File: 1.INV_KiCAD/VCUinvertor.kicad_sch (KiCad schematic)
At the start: 156 parts, among them J10 FAN2, J11 PUMP1, J12 PUMP2, J7 PowerSupply, J8 FAN1, J9 BRAKE LIGHT, K1 IM06DGR, Q1 2N7002, Q10 2N7002, Q11 2N7002, Q12 2N7002, Q13 BC848C, Q14 2N7002, Q15 IRLZ44N, Q16 IRLZ44N, Q17 IRLZ44N, Q18 2N7002, Q19 IRLZ44N, Q2 2N7002, Q3 2N7002, Q4 2N7002, Q5 2N7002, Q6 2N7002, Q7 2N7002, Q8 2N7002, Q9 2N7002, U1 TJA1448ATK, U2 REF3433T, U3 TLV76150DCY

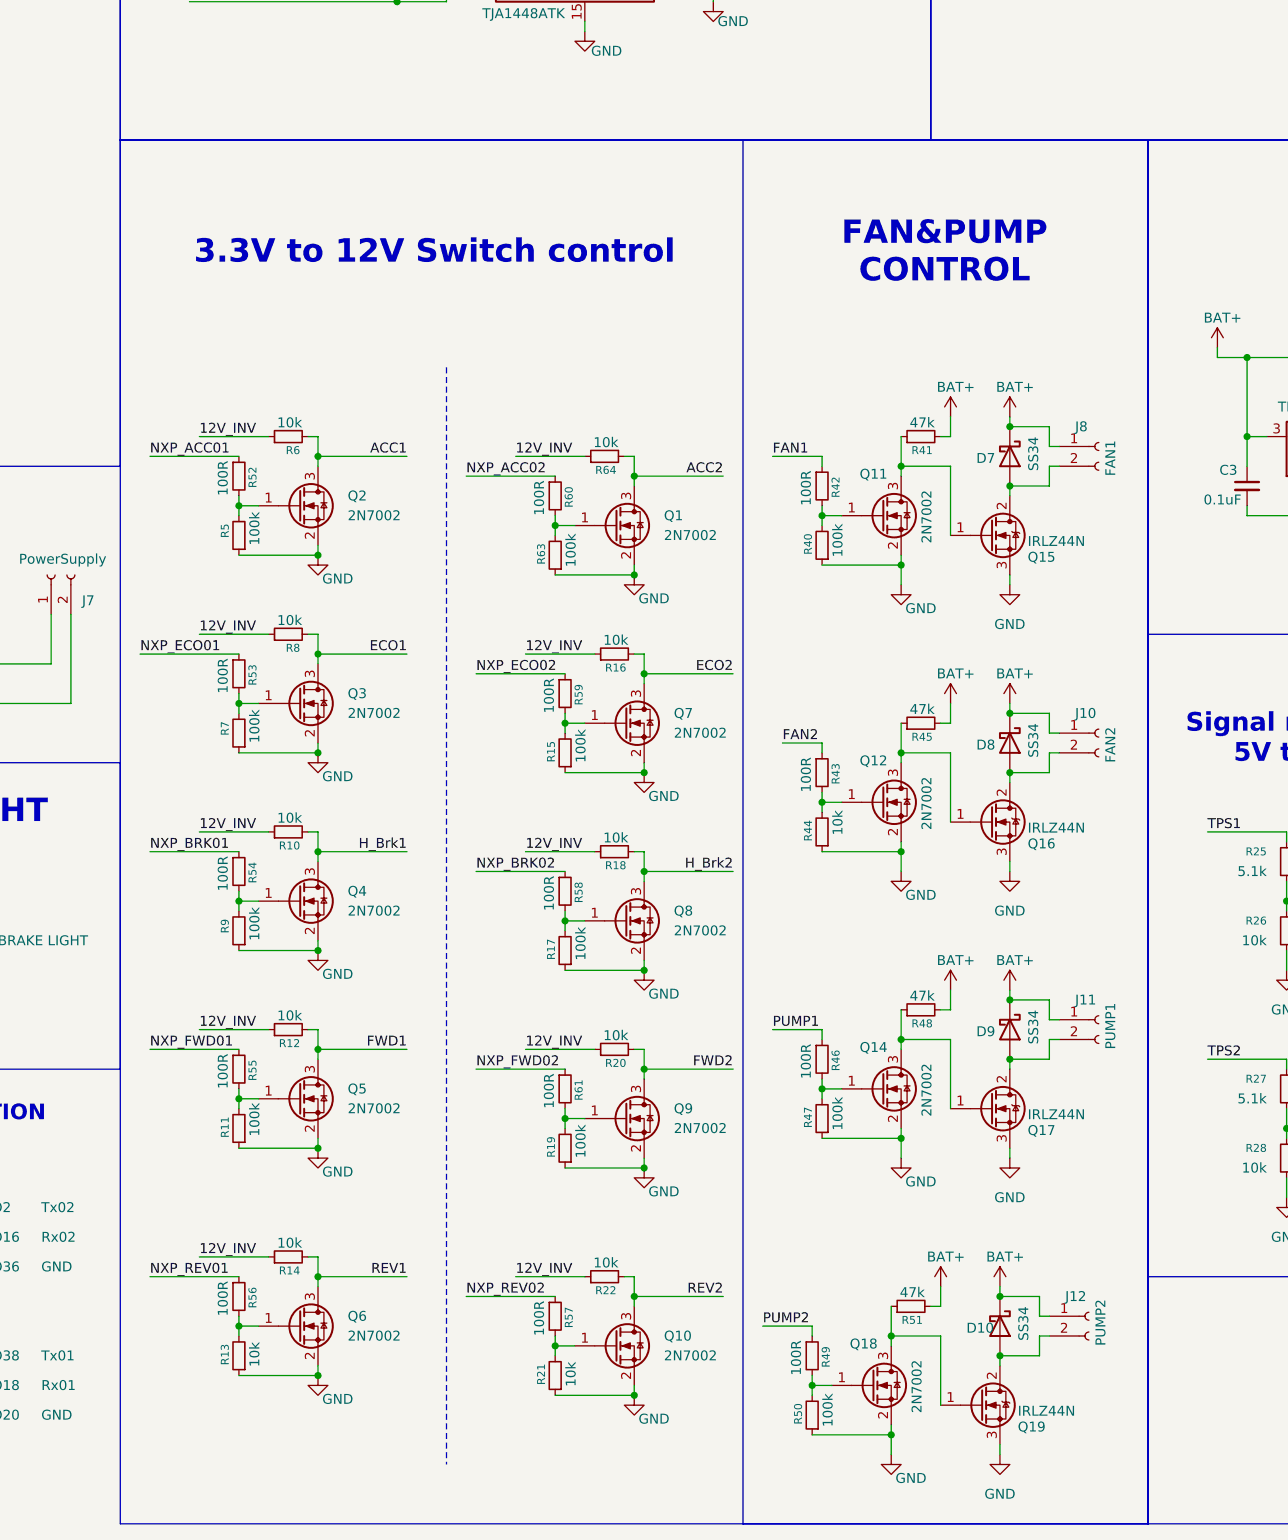
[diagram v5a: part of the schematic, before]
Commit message: Gate Driver MOS added + layout done
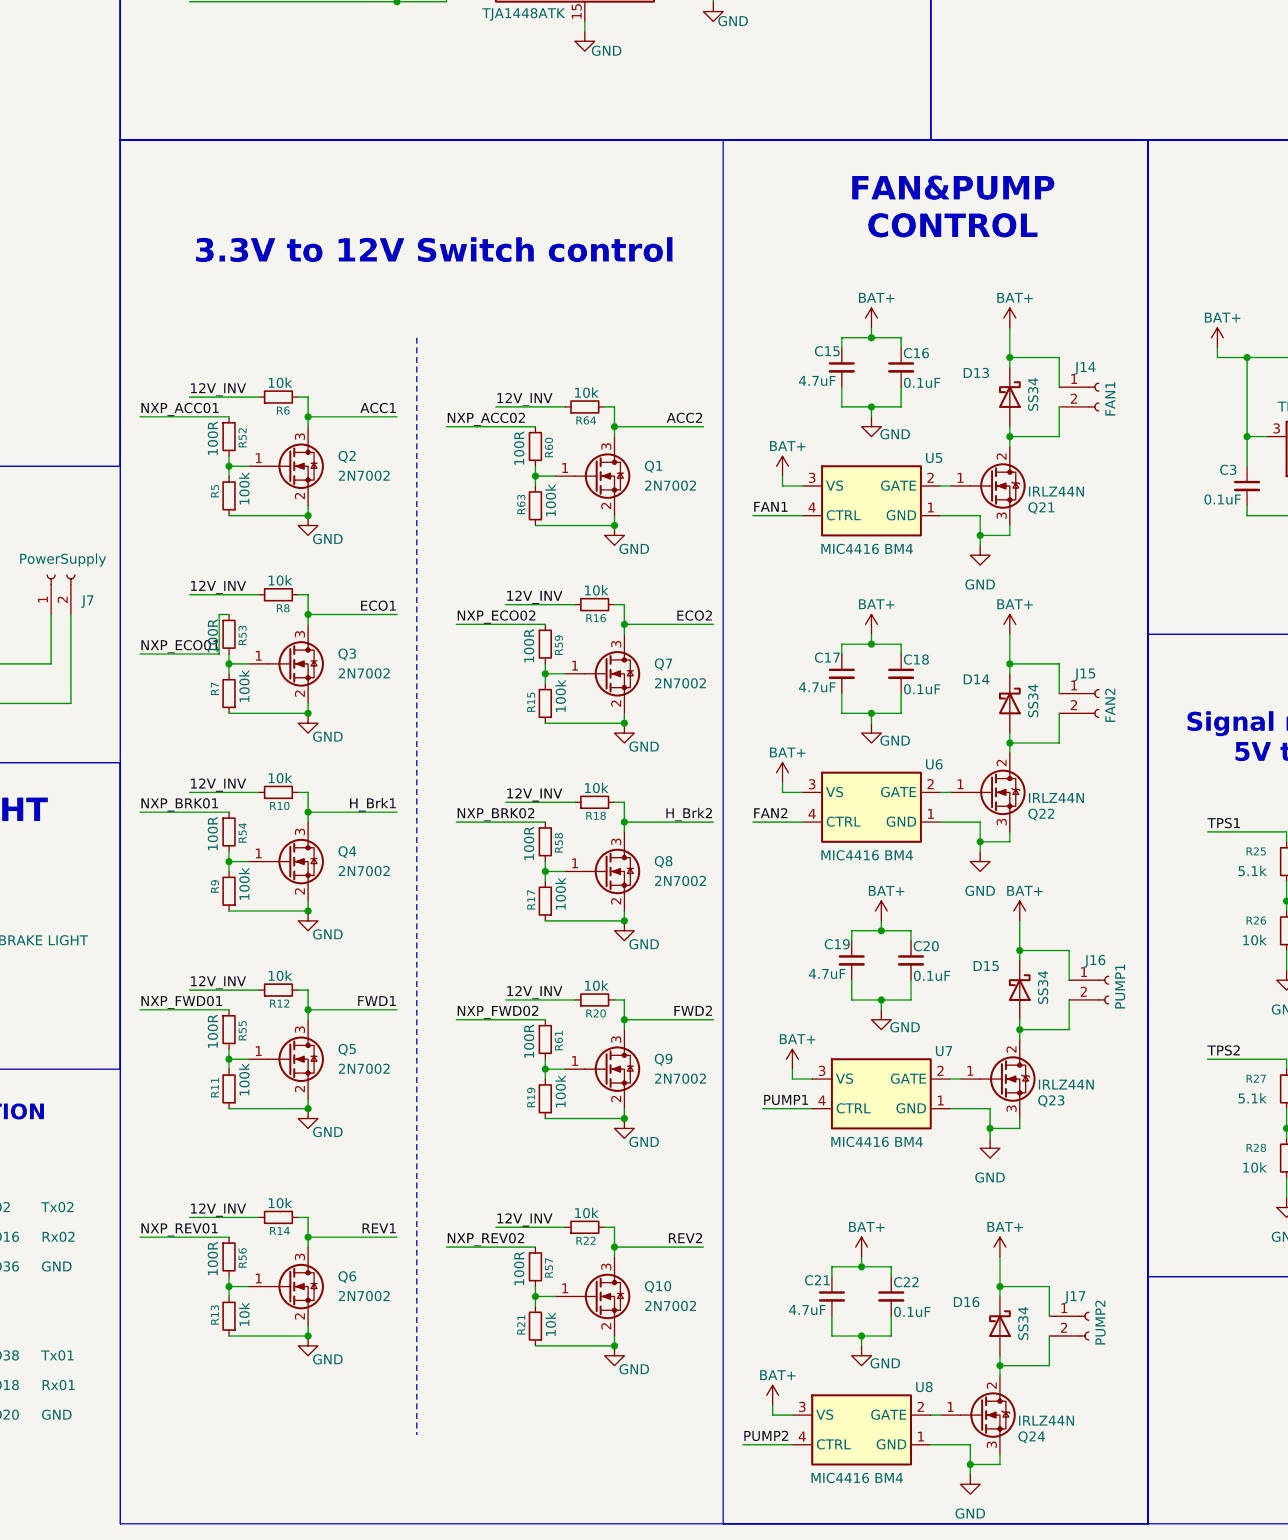
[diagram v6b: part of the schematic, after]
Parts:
- removed D10, D7, D8, D9: SS34, Diode_SMD:D_SMA, symbol Diode:SS34
- removed J10: FAN2, Connector_JST:JST_XH_B2B-XH-A_1x02_P2.50mm_Vertical, symbol Connector:Conn_01x02_Socket
- removed J11: PUMP1, Connector_JST:JST_XH_B2B-XH-A_1x02_P2.50mm_Vertical, symbol Connector:Conn_01x02_Socket
- removed J12: PUMP2, Connector_JST:JST_XH_B2B-XH-A_1x02_P2.50mm_Vertical, symbol Connector:Conn_01x02_Socket
- removed J8: FAN1, Connector_JST:JST_XH_B2B-XH-A_1x02_P2.50mm_Vertical, symbol Connector:Conn_01x02_Socket
- removed Q11, Q12, Q14, Q18: 2N7002, Package_TO_SOT_SMD:SOT-23, symbol Transistor_FET:2N7002
- removed Q15, Q16, Q17, Q19: IRLZ44N, Package_TO_SOT_THT:TO-220-3_Vertical, symbol Transistor_FET:IRLZ44N
- removed R40, R47, R50: 100k, Resistor_SMD:R_1206_3216Metric_Pad1.30x1.75mm_HandSolder, symbol Device:R_Small
- removed R41, R45, R48, R51: 47k, Resistor_SMD:R_1206_3216Metric_Pad1.30x1.75mm_HandSolder, symbol Device:R_Small
- removed R42, R43, R46, R49: 100R, Resistor_SMD:R_1206_3216Metric_Pad1.30x1.75mm_HandSolder, symbol Device:R_Small
- removed R44: 10k, Resistor_SMD:R_1206_3216Metric_Pad1.30x1.75mm_HandSolder, symbol Device:R_Small
- added C15, C17, C19, C21: 4.7uF, Capacitor_SMD:C_1206_3216Metric_Pad1.33x1.80mm_HandSolder, symbol Device:C_Small
- added C16, C18, C20, C22: 0.1uF, Capacitor_SMD:C_1206_3216Metric_Pad1.33x1.80mm_HandSolder, symbol Device:C_Small
- added D13, D14, D15, D16: SS34, Diode_SMD:D_SMA, symbol Diode:SS34
- added J14: FAN1, Connector_JST:JST_XH_B2B-XH-A_1x02_P2.50mm_Vertical, symbol Connector:Conn_01x02_Socket
- added J15: FAN2, Connector_JST:JST_XH_B2B-XH-A_1x02_P2.50mm_Vertical, symbol Connector:Conn_01x02_Socket
- added J16: PUMP1, Connector_JST:JST_XH_B2B-XH-A_1x02_P2.50mm_Vertical, symbol Connector:Conn_01x02_Socket
- added J17: PUMP2, Connector_JST:JST_XH_B2B-XH-A_1x02_P2.50mm_Vertical, symbol Connector:Conn_01x02_Socket
- added Q21, Q22, Q23, Q24: IRLZ44N, Package_TO_SOT_THT:TO-220-3_Vertical, symbol Transistor_FET:IRLZ44N
- added U5, U6, U7, U8: MIC4416 BM4, Package_TO_SOT_SMD:SOT-143_Handsoldering, symbol Driver_FET:MIC4426
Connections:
- net BAT+: now also C15.1, C16.1, C17.1, C18.1, C19.1, C20.1, C21.1, C22.1, D13.1 (K), D14.1 (K), D15.1 (K), D16.1 (K), J14.1 (Pin_1), J15.1 (Pin_1), J16.1 (Pin_1), J17.1 (Pin_1), U5.3 (VS), U6.3 (VS), U7.3 (VS), U8.3 (VS)
- net FAN1: now also U5.4 (CTRL)
- net FAN2: now also U6.4 (CTRL)
- net GND: now also C15.2, C16.2, C17.2, C18.2, C19.2, C20.2, C21.2, C22.2, Q21.3 (S), Q22.3 (S), Q23.3 (S), Q24.3 (S), U5.1 (GND), U6.1 (GND), U7.1 (GND), U8.1 (GND)
- net PUMP1: now also U7.4 (CTRL)
- net PUMP2: now also U8.4 (CTRL)
- new net: Q24.1 (G), U8.2 (GATE)
- new net: D16.2 (A), J17.2 (Pin_2), Q24.2 (D)
- new net: Q23.1 (G), U7.2 (GATE)
- new net: D15.2 (A), J16.2 (Pin_2), Q23.2 (D)
- new net: Q21.1 (G), U5.2 (GATE)
- new net: D14.2 (A), J15.2 (Pin_2), Q22.2 (D)
- new net: Q22.1 (G), U6.2 (GATE)
- new net: D13.2 (A), J14.2 (Pin_2), Q21.2 (D)
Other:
- moved on the sheet: Q1, Q10, Q2, Q3, Q4, Q5, Q6, Q7, Q8, Q9, R10, R11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

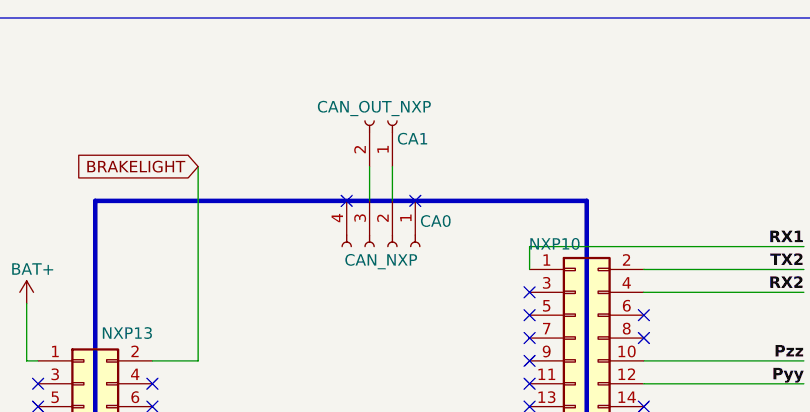
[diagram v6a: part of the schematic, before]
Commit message: CAN_IN + CAN_OUT added
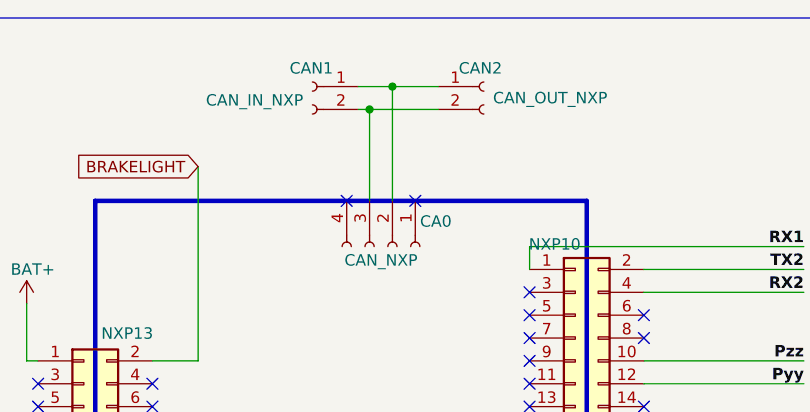
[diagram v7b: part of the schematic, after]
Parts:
- added CAN2: CAN_OUT_NXP, Connector_JST:JST_PH_B2B-PH-K_1x02_P2.00mm_Vertical, symbol Connector:Conn_01x02_Socket
- CAN1: renamed from CA1; value CAN_OUT_NXP -> CAN_IN_NXP; footprint Connector_JST:JST_XH_B2B-XH-A_1x02_P2.50mm_Vertical -> Connector_JST:JST_PH_B2B-PH-K_1x02_P2.00mm_Vertical
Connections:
- net at CA0.2 (Pin_2), CAN1.1 (Pin_1): now also CAN2.1 (Pin_1)
- net at CA0.3 (Pin_3), CAN1.2 (Pin_2): now also CAN2.2 (Pin_2)
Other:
- moved on the sheet: CAN1
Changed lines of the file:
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@@
 	)
 	(junction
+		(at 93.98 20.32)
+		(diameter 0)
+		(color 0 0 0 0)
+	)
+	(junction
 		(at 201.93 64.77)
 		(diameter 0)
@@
 	)
 	(junction
+		(at 91.44 22.86)
+		(diameter 0)
+		(color 0 0 0 0)
+	)
+	(junction
 		(at 191.77 167.64)
 		(diameter 0)
@@
 	(wire
 		(pts
+			(xy 90.17 20.32) (xy 93.98 20.32)
+		)
+		(stroke
+			(width 0)
+			(type default)
+		)
+	)
+	(wire
+		(pts
 			(xy 109.22 38.1) (xy 139.7 38.1)
 		)
@@
 	(wire
 		(pts
-			(xy 91.44 29.21) (xy 91.44 33.02)
-		)
-		(stroke
-			(width 0)
-			(type default)
-		)
-	)
-	(wire
-		(pts
 			(xy 232.41 219.71) (xy 232.41 220.98)
 		)
@@
 	(wire
 		(pts
+			(xy 91.44 22.86) (xy 91.44 33.02)
+		)
+		(stroke
+			(width 0)
+			(type default)
+		)
+	)
+	(wire
+		(pts
 			(xy 353.06 73.66) (xy 358.14 73.66)
 		)
@@
 	(wire
 		(pts
+			(xy 90.17 22.86) (xy 91.44 22.86)
+		)
+		(stroke
+			(width 0)
+			(type default)
+		)
+	)
+	(wire
+		(pts
 			(xy 181.61 154.94) (xy 191.77 154.94)
 		)
@@
 	(wire
 		(pts
+			(xy 91.44 22.86) (xy 99.06 22.86)
+		)
+		(stroke
+			(width 0)
+			(type default)
+		)
+	)
+	(wire
+		(pts
 			(xy 355.6 224.79) (xy 355.6 227.33)
 		)
@@
 	(wire
 		(pts
+			(xy 93.98 20.32) (xy 93.98 33.02)
+		)
+		(stroke
+			(width 0)
+			(type default)
+		)
+	)
+	(wire
+		(pts
 			(xy 127 167.64) (xy 140.97 167.64)
 		)
@@
 	(wire
 		(pts
+			(xy 93.98 20.32) (xy 99.06 20.32)
+		)
+		(stroke
+			(width 0)
+			(type default)
+		)
+	)
+	(wire
+		(pts
 			(xy 25.4 215.9) (xy 25.4 219.71)
 		)
@@
 	(wire
 		(pts
-			(xy 93.98 29.21) (xy 93.98 33.02)
-		)
-		(stroke
-			(width 0)
-			(type default)
-		)
-	)
-	(wire
-		(pts
 			(xy 210.82 168.91) (xy 222.25 168.91)
 		)
@@
 	(symbol
 		(lib_id "Connector:Conn_01x02_Socket")
-		(at 93.98 24.13 270)
-		(mirror x)
+		(at 85.09 20.32 0)
+		(mirror y)
 		(unit 1)
 		(body_style 1)
@@
 		(in_pos_files yes)
 		(dnp no)
-		(property "Reference" "CA1"
-			(at 94.488 26.162 90)
+		(property "Reference" "CAN1"
+			(at 87.376 18.288 0)
 			(show_name no)
 			(do_not_autoplace no)
@@
 			)
 		)
-		(property "Value" "CAN_OUT_NXP"
-			(at 85.598 22.606 90)
+		(property "Value" "CAN_IN_NXP"
+			(at 84.074 21.844 0)
 			(show_name no)
 			(do_not_autoplace no)
@@
 			)
 		)
-		(property "Footprint" "Connector_JST:JST_XH_B2B-XH-A_1x02_P2.50mm_Vertical"
-			(at 93.98 24.13 0)
+		(property "Footprint" "Connector_JST:JST_PH_B2B-PH-K_1x02_P2.00mm_Vertical"
+			(at 85.09 20.32 0)
 			(hide yes)
 			(show_name no)
@@
 		)
 		(property "Datasheet" ""
-			(at 93.98 24.13 0)
+			(at 85.09 20.32 0)
 			(hide yes)
 			(show_name no)
@@
 		)
 		(property "Description" "Generic connector, single row, 01x02, script generated"
-			(at 93.98 24.13 0)
+			(at 85.09 20.32 0)
 			(hide yes)
 			(show_name no)
@@
 			(project "VCUinvertor"
 				(path "/2b4b6758-f217-4dbc-8f9c-9ada5d4e488c"
-					(reference "CA1")
+					(reference "CAN1")
 					(unit 1)
 				)
@@
 					(unit 1)
 				)
+			)
+		)
+	)
+	(symbol
+		(lib_id "Connector:Conn_01x02_Socket")
+		(at 104.14 20.32 0)
+		(unit 1)
+		(body_style 1)
+		(exclude_from_sim no)
+		(in_bom yes)
+		(on_board yes)
+		(in_pos_files yes)
+		(dnp no)
+		(property "Reference" "CAN2"
+			(at 101.346 18.288 0)
+			(show_name no)
+			(do_not_autoplace no)
+			(effects
+				(font
+					(size 1.27 1.27)
+				)
+				(justify left)
+			)
+		)
+		(property "Value" "CAN_OUT_NXP"
+			(at 105.156 21.59 0)
+			(show_name no)
+			(do_not_autoplace no)
+			(effects
+				(font
+					(size 1.27 1.27)
+				)
+				(justify left)
+			)
+		)
+		(property "Footprint" "Connector_JST:JST_PH_B2B-PH-K_1x02_P2.00mm_Vertical"
+			(at 104.14 20.32 0)
+			(hide yes)
+			(show_name no)
+			(do_not_autoplace no)
+			(effects
+				(font
+					(size 1.27 1.27)
+				)
+			)
+		)
+		(property "Datasheet" ""
+			(at 104.14 20.32 0)
+			(hide yes)
+			(show_name no)
+			(do_not_autoplace no)
+			(effects
+				(font
+					(size 1.27 1.27)
+				)
+			)
+		)
+		(property "Description" "Generic connector, single row, 01x02, script generated"
+			(at 104.14 20.32 0)
+			(hide yes)
+			(show_name no)
+			(do_not_autoplace no)
+			(effects
+				(font
+					(size 1.27 1.27)
+				)
+			)
+		)
+		(pin "1"
+		)
+		(pin "2"
+		)
+		(instances
+			(project "VCUinvertor"
+				(path "/2b4b6758-f217-4dbc-8f9c-9ada5d4e488c"
+					(reference "CAN2")
+					(unit 1)
+				)

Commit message: TEMP/PRESSURE ctrl schematic - proto
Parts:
- added C13: 0.1uF, Capacitor_SMD:C_1206_3216Metric_Pad1.33x1.80mm_HandSolder, symbol Device:C_Small
- added P1: PRESSURE SENSOR 1, Connector_JST:JST_XH_B3B-XH-A_1x03_P2.50mm_Vertical, symbol Connector:Conn_01x03_Socket
- added P2: PRESSURE SENSOR 2, Connector_JST:JST_XH_B3B-XH-A_1x03_P2.50mm_Vertical, symbol Connector:Conn_01x03_Socket
- added R62, R65, R66, R67, R68: 10k, Resistor_SMD:R_0805_2012Metric, symbol Device:R_Small
- added TEMP1: NTC1, Connector_JST:JST_PH_B2B-PH-K_1x02_P2.00mm_Vertical, symbol Connector:Conn_01x02_Socket
- added TEMP2: NTC2, Connector_JST:JST_PH_B2B-PH-K_1x02_P2.00mm_Vertical, symbol Connector:Conn_01x02_Socket
- added U4: ADS1115, Package_SO:TSSOP-10_3x3mm_P0.5mm, symbol Analog_ADC:ADS1115IDGS
- renumbered J9 to BR1
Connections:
- net +5V: now also C13.1, P1.3 (Pin_3), P2.3 (Pin_3), R62.1, R65.1, R66.1, R67.1, U4.8 (VDD)
- net GND: now also C13.2, P1.1 (Pin_1), P2.1 (Pin_1), R68.2, TEMP1.1 (Pin_1), TEMP2.1 (Pin_1), U4.3 (GND)
- new net: R68.1, U4.1 (ADDR)
- new net ADS_SCL: R66.2, U4.10 (SCL)
- new net ADS_SDA: R67.2, U4.9 (SDA)
- new net PRES1: P1.2 (Pin_2), U4.6 (AIN2)
- new net PRES2: P2.2 (Pin_2), U4.7 (AIN3)
- new net TEMP1: R62.2, TEMP1.2 (Pin_2), U4.4 (AIN0)
- new net TEMP2: R65.2, TEMP2.2 (Pin_2), U4.5 (AIN1)
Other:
- note added: "ADS1115 base configuration"
- note added: "Analog input"
- note added: "I2C"
- note added: "NTC sensor Temp measure"
- note added: "Pressure sensors"
- moved on the sheet: 3.3V1, 5V1, BR1, C1, C11, C15, C16, C17, C18, C19, C2, C20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
